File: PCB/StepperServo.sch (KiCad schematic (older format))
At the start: 78 parts, among them P1 Conn_01x06, P2 Conn_01x04, P4 Conn_01x08, P5 Conn_01x02, U1 BNOR11, U2 A4950E, U3 EL-0631, U4 A4950E, U5 TLE5012B, U6 EL357NC, U7 STM32F103CBTx, U8 LD1117S33CTR, U9 PCA82C251, Y1 Crystal, p7 Conn_01x08

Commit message: Added misssing footprints to pcb
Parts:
- U1: footprint (none) -> Package_TO_SOT_SMD:SOT-23-6
- U8: footprint digikey-footprints:SOT-223 -> Package_TO_SOT_SMD:SOT-223; symbol StepperServo-rescue:LD1117S33CTR-dk_PMIC-Voltage-Regulators-Linear-BTTS57Bv2-rescue -> StepperServo-rescue:LD1117S33CTR-dk_PMIC-Voltage-Regulators-Linear
- Y1: footprint (none) -> Crystal:Crystal_SMD_EuroQuartz_MT-4Pin_3.2x2.5mm_HandSoldering; symbol StepperServo-rescue:Crystal-Device-BTTS57Bv2-rescue -> StepperServo-rescue:Crystal-Device
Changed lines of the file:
@@
 Text GLabel 7300 4000 0    50   Input ~ 0
 MICROSTEP1_SW
-Text GLabel 10750 2450 2    50   Input ~ 0
-STP_IN
-Text GLabel 10750 2600 2    50   Input ~ 0
-DIR_IN
-Text GLabel 10300 3400 2    50   Input ~ 0
-EN_IN
 Text GLabel 7300 4200 0    50   Output ~ 0
 OLED_CS
@@
 Text GLabel 7300 3600 0    50   Input ~ 0
 motordriverU4#3
-$Comp
-L StepperServo-rescue:R-Device-BTTS57Bv2-rescue R5
-U 1 1 60AA734D
-P 9500 3050
-F 0 "R5" V 9600 3050 50  0000 C CNN
-F 1 "?R" V 9500 3050 50  0000 C CNN
-F 2 "Resistor_SMD:R_0603_1608Metric" V 9430 3050 50  0001 C CNN
-F 3 "~" H 9500 3050 50  0001 C CNN
-	1    9500 3050
-	-1   0    0    1
-$EndComp
-$Comp
-L StepperServo-rescue:R-Device-BTTS57Bv2-rescue R12
-U 1 1 60AC6CB6
-P 10150 3400
-F 0 "R12" V 10250 3400 50  0000 C CNN
-F 1 "?R" V 10150 3400 50  0000 C CNN
-F 2 "Resistor_SMD:R_0805_2012Metric" V 10080 3400 50  0001 C CNN
-F 3 "~" H 10150 3400 50  0001 C CNN
-	1    10150 3400
-	0    -1   -1   0
-$EndComp
-Connection ~ 9500 3200
-Wire Wire Line
-	9500 3200 9600 3200
 Text GLabel 8050 1550 1    50   Input ~ 0
 VDD
@@
 	8100 1650 8100 1700
 Wire Wire Line
-	8600 3200 9500 3200
-Wire Wire Line
 	8050 1650 8050 1550
 Connection ~ 8050 1650
@@
 Wire Wire Line
 	7900 1650 8000 1650
-Text GLabel 9500 2900 1    50   Input ~ 0
-VDD
-Text GLabel 9600 3400 0    50   Input ~ 0
-VSS
 Wire Wire Line
 	8100 1650 8200 1650
@@
 	8200 1650 8200 1700
 Connection ~ 8100 1650
-$Comp
-L StepperServo-rescue:R-Device-BTTS57Bv2-rescue R9
-U 1 1 60ACF7F8
-P 10600 2600
-F 0 "R9" V 10700 2600 50  0000 C CNN
-F 1 "?R" V 10600 2600 50  0000 C CNN
-F 2 "Resistor_SMD:R_0805_2012Metric" V 10530 2600 50  0001 C CNN
-F 3 "~" H 10600 2600 50  0001 C CNN
-	1    10600 2600
-	0    -1   -1   0
-$EndComp
-$Comp
-L StepperServo-rescue:R-Device-BTTS57Bv2-rescue R3
-U 1 1 60AD1627
-P 10600 2450
-F 0 "R3" V 10700 2450 50  0000 C CNN
-F 1 "?R" V 10600 2500 50  0000 C CNN
-F 2 "Resistor_SMD:R_0805_2012Metric" V 10530 2450 50  0001 C CNN
-F 3 "~" H 10600 2450 50  0001 C CNN
-	1    10600 2450
-	0    -1   -1   0
-$EndComp
-$Comp
-L StepperServo-rescue:R-Device-BTTS57Bv2-rescue R8
-U 1 1 60AEAB54
-P 9600 2200
-F 0 "R8" V 9700 2200 50  0000 C CNN
-F 1 "?R" V 9600 2200 50  0000 C CNN
-F 2 "Resistor_SMD:R_0603_1608Metric" V 9530 2200 50  0001 C CNN
-F 3 "~" H 9600 2200 50  0001 C CNN
-	1    9600 2200
-	-1   0    0    1
-$EndComp
 $Comp
 L StepperServo-rescue:R-Device-BTTS57Bv2-rescue R15
@@
 Text GLabel 9350 2050 1    50   Input ~ 0
 VDD
-Text GLabel 9600 2050 1    50   Input ~ 0
-VDD
-Text GLabel 9900 2250 0    50   Input ~ 0
-VSS
 $Comp
 L StepperServo-rescue:LED-Device-BTTS57Bv2-rescue D4
@@
 	1    0    0    -1
 $EndComp
-$Comp
-L el-0631:EL-0631 U3
-U 1 1 60A729DF
-P 10350 3050
-F 0 "U3" H 10525 4075 50  0000 C CNN
-F 1 "EL-0631" H 10525 3984 50  0000 C CNN
-F 2 "Package_SO:SOP-8_3.9x4.9mm_P1.27mm" H 9990 2730 50  0001 C CNN
-F 3 "" H 9990 2730 50  0001 C CNN
-	1    10350 3050
-	-1   0    0    -1
-$EndComp
 Wire Wire Line
 	9350 2350 9350 2450
-$Comp
-L el-0631:EL357NC U6
-U 1 1 60AC06ED
-P 9850 3550
-F 0 "U6" H 9900 4125 50  0000 C CNN
-F 1 "EL357NC" H 9900 4034 50  0000 C CNN
-F 2 "Package_SO:SOP-4_3.8x4.1mm_P2.54mm" H 9850 3550 50  0001 C CNN
-F 3 "" H 9850 3550 50  0001 C CNN
-	1    9850 3550
-	-1   0    0    -1
-$EndComp
-Wire Wire Line
-	9600 2350 9600 2600
 $Comp
 L StepperServo-rescue:C-Device-BTTS57Bv2-rescue C3
@@
 $EndComp
 $Comp
-L StepperServo-rescue:Crystal-Device-BTTS57Bv2-rescue Y1
+L StepperServo-rescue:Crystal-Device Y1
 U 1 1 60B8D3A3
 P 5000 2350
 F 0 "Y1" H 5000 2618 50  0000 C CNN
 F 1 "Crystal" H 5000 2527 50  0000 C CNN
-F 2 "" H 5000 2350 50  0001 C CNN
+F 2 "Crystal:Crystal_SMD_EuroQuartz_MT-4Pin_3.2x2.5mm_HandSoldering" H 5000 2350 50  0001 C CNN
 F 3 "~" H 5000 2350 50  0001 C CNN
 	1    5000 2350
@@
 $EndComp
 $Comp
-L StepperServo-rescue:LD1117S33CTR-dk_PMIC-Voltage-Regulators-Linear-BTTS57Bv2-rescue U8
+L StepperServo-rescue:LD1117S33CTR-dk_PMIC-Voltage-Regulators-Linear U8
 U 1 1 60BA0B17
 P 1500 4100
 F 0 "U8" H 1550 4387 60  0000 C CNN
 F 1 "LD1117S33CTR" H 1550 4281 60  0000 C CNN
-F 2 "digikey-footprints:SOT-223" H 1700 4300 60  0001 L CNN
+F 2 "Package_TO_SOT_SMD:SOT-223" H 1700 4300 60  0000 L CNN
 F 3 "http://www.st.com/content/ccc/resource/technical/document/datasheet/99/3b/7d/91/91/51/4b/be/CD00000544.pdf/files/CD00000544.pdf/jcr:content/translations/en.CD00000544.pdf" H 1700 4400 60  0001 L CNN
 F 4 "497-1241-1-ND" H 1700 4500 60  0001 L CNN "Digi-Key_PN"
@@
 F 0 "U1" H 2500 6025 50  0000 C CNN
 F 1 "BNOR11" H 2500 5934 50  0000 C CNN
-F 2 "" H 2450 5450 50  0001 C CNN
+F 2 "Package_TO_SOT_SMD:SOT-23-6" H 2450 5450 50  0001 C CNN
 F 3 "" H 2450 5450 50  0001 C CNN
 	1    2450 5450
@@
 	9150 2450 9350 2450
 Wire Wire Line
-	9350 2450 9900 2450
-Connection ~ 9350 2450
-Wire Wire Line
 	9300 3100 9300 2600
-Wire Wire Line
-	9300 2600 9600 2600
-Wire Wire Line
-	9600 2600 9900 2600
-Connection ~ 9600 2600
 $Comp
 L Mechanical:MountingHole_Pad H1
@@
 Wire Wire Line
 	2300 5900 2300 6050
-Text GLabel 9900 2800 0    50   Input ~ 0
-VDD
 Text GLabel 7500 6200 0    50   Input ~ 0
+com
+Wire Wire Line
+	8600 3000 9150 3000
+Wire Wire Line
+	8600 3100 9300 3100
+Connection ~ 9350 2450
+Text GLabel 10450 2800 2    50   Input ~ 0
+com
+Text GLabel 10450 2250 2    50   Input ~ 0
 com
 Text GLabel 10000 3200 2    50   Input ~ 0
 com
-Text GLabel 10450 2250 2    50   Input ~ 0
-com
-Text GLabel 10450 2800 2    50   Input ~ 0
-com
-Wire Wire Line
-	8600 3000 9150 3000
-Wire Wire Line
-	8600 3100 9300 3100
+Text GLabel 9900 2800 0    50   Input ~ 0
+VDD
+Connection ~ 9600 2600
+Wire Wire Line
+	9600 2600 9900 2600
+Wire Wire Line
+	9300 2600 9600 2600
+Wire Wire Line
+	9350 2450 9900 2450
+Wire Wire Line
+	9600 2350 9600 2600
+$Comp
+L el-0631:EL357NC U6
+U 1 1 60AC06ED
+P 9850 3550
+F 0 "U6" H 9900 4125 50  0000 C CNN
+F 1 "EL357NC" H 9900 4034 50  0000 C CNN
+F 2 "Package_SO:SOP-4_3.8x4.1mm_P2.54mm" H 9850 3550 50  0001 C CNN
+F 3 "" H 9850 3550 50  0001 C CNN
+	1    9850 3550
+	-1   0    0    -1
+$EndComp
+$Comp
+L el-0631:EL-0631 U3
+U 1 1 60A729DF
+P 10350 3050
+F 0 "U3" H 10525 4075 50  0000 C CNN
+F 1 "EL-0631" H 10525 3984 50  0000 C CNN
+F 2 "Package_SO:SOP-8_3.9x4.9mm_P1.27mm" H 9990 2730 50  0001 C CNN
+F 3 "" H 9990 2730 50  0001 C CNN
+	1    10350 3050
+	-1   0    0    -1
+$EndComp
+Text GLabel 9900 2250 0    50   Input ~ 0
+VSS
+Text GLabel 9600 2050 1    50   Input ~ 0
+VDD
+$Comp
+L StepperServo-rescue:R-Device-BTTS57Bv2-rescue R8
+U 1 1 60AEAB54
+P 9600 2200
+F 0 "R8" V 9700 2200 50  0000 C CNN
+F 1 "?R" V 9600 2200 50  0000 C CNN
+F 2 "Resistor_SMD:R_0603_1608Metric" V 9530 2200 50  0001 C CNN
+F 3 "~" H 9600 2200 50  0001 C CNN
+	1    9600 2200
+	-1   0    0    1
+$EndComp
+$Comp
+L StepperServo-rescue:R-Device-BTTS57Bv2-rescue R3
+U 1 1 60AD1627
+P 10600 2450
+F 0 "R3" V 10700 2450 50  0000 C CNN
+F 1 "?R" V 10600 2500 50  0000 C CNN
+F 2 "Resistor_SMD:R_0805_2012Metric" V 10530 2450 50  0001 C CNN
+F 3 "~" H 10600 2450 50  0001 C CNN
+	1    10600 2450
+	0    -1   -1   0
+$EndComp
+$Comp
+L StepperServo-rescue:R-Device-BTTS57Bv2-rescue R9
+U 1 1 60ACF7F8
+P 10600 2600
+F 0 "R9" V 10700 2600 50  0000 C CNN
+F 1 "?R" V 10600 2600 50  0000 C CNN
+F 2 "Resistor_SMD:R_0805_2012Metric" V 10530 2600 50  0001 C CNN
+F 3 "~" H 10600 2600 50  0001 C CNN
+	1    10600 2600
+	0    -1   -1   0
+$EndComp
+Text GLabel 9600 3400 0    50   Input ~ 0
+VSS
+Text GLabel 9500 2900 1    50   Input ~ 0
+VDD
+Wire Wire Line
+	8600 3200 9500 3200
+Wire Wire Line
+	9500 3200 9600 3200
+Connection ~ 9500 3200
+$Comp
+L StepperServo-rescue:R-Device-BTTS57Bv2-rescue R12
+U 1 1 60AC6CB6
+P 10150 3400
+F 0 "R12" V 10250 3400 50  0000 C CNN
+F 1 "?R" V 10150 3400 50  0000 C CNN
+F 2 "Resistor_SMD:R_0805_2012Metric" V 10080 3400 50  0001 C CNN
+F 3 "~" H 10150 3400 50  0001 C CNN
+	1    10150 3400
+	0    -1   -1   0
+$EndComp
+$Comp
+L StepperServo-rescue:R-Device-BTTS57Bv2-rescue R5
+U 1 1 60AA734D
+P 9500 3050
+F 0 "R5" V 9600 3050 50  0000 C CNN
+F 1 "?R" V 9500 3050 50  0000 C CNN
+F 2 "Resistor_SMD:R_0603_1608Metric" V 9430 3050 50  0001 C CNN
+F 3 "~" H 9500 3050 50  0001 C CNN
+	1    9500 3050
+	-1   0    0    1
+$EndComp
+Text GLabel 10300 3400 2    50   Input ~ 0
+EN_IN
+Text GLabel 10750 2600 2    50   Input ~ 0
+DIR_IN
+Text GLabel 10750 2450 2    50   Input ~ 0
+STP_IN
 $EndSCHEMATC

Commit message: Removed dir, step, enable
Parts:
- removed R12, R3, R9: ?R, Resistor_SMD:R_0805_2012Metric, symbol StepperServo-rescue:R-Device-BTTS57Bv2-rescue
- removed R15, R5, R8: ?R, Resistor_SMD:R_0603_1608Metric, symbol StepperServo-rescue:R-Device-BTTS57Bv2-rescue
- removed U3: EL-0631, Package_SO:SOP-8_3.9x4.9mm_P1.27mm, symbol el-0631:EL-0631
- removed U6: EL357NC, Package_SO:SOP-4_3.8x4.1mm_P2.54mm, symbol el-0631:EL357NC
- P1: footprint Connector_JST:JST_XH_B6B-XH-A_1x06_P2.50mm_Vertical -> Connector_JST:JST_XH_B2B-XH-A_1x02_P2.50mm_Vertical; symbol StepperServo-rescue:Conn_01x06-Connector_Generic-BTTS57Bv2-rescue -> Connector_Generic:Conn_01x02
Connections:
- net DIR_IN is gone; now on net GND: P1.1 (Pin_1)
- net STP_IN is gone; now on net VMOT: P1.2 (Pin_2)
- net GND: no longer P1.4 (Pin_4)
- net VMOT: no longer P1.6 (Pin_6)
- removed net EN_IN: P1.3 (Pin_3)
- removed net com: P1.5 (Pin_5)
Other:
- moved on the sheet: C13, C16, C2, C4, Next-K2

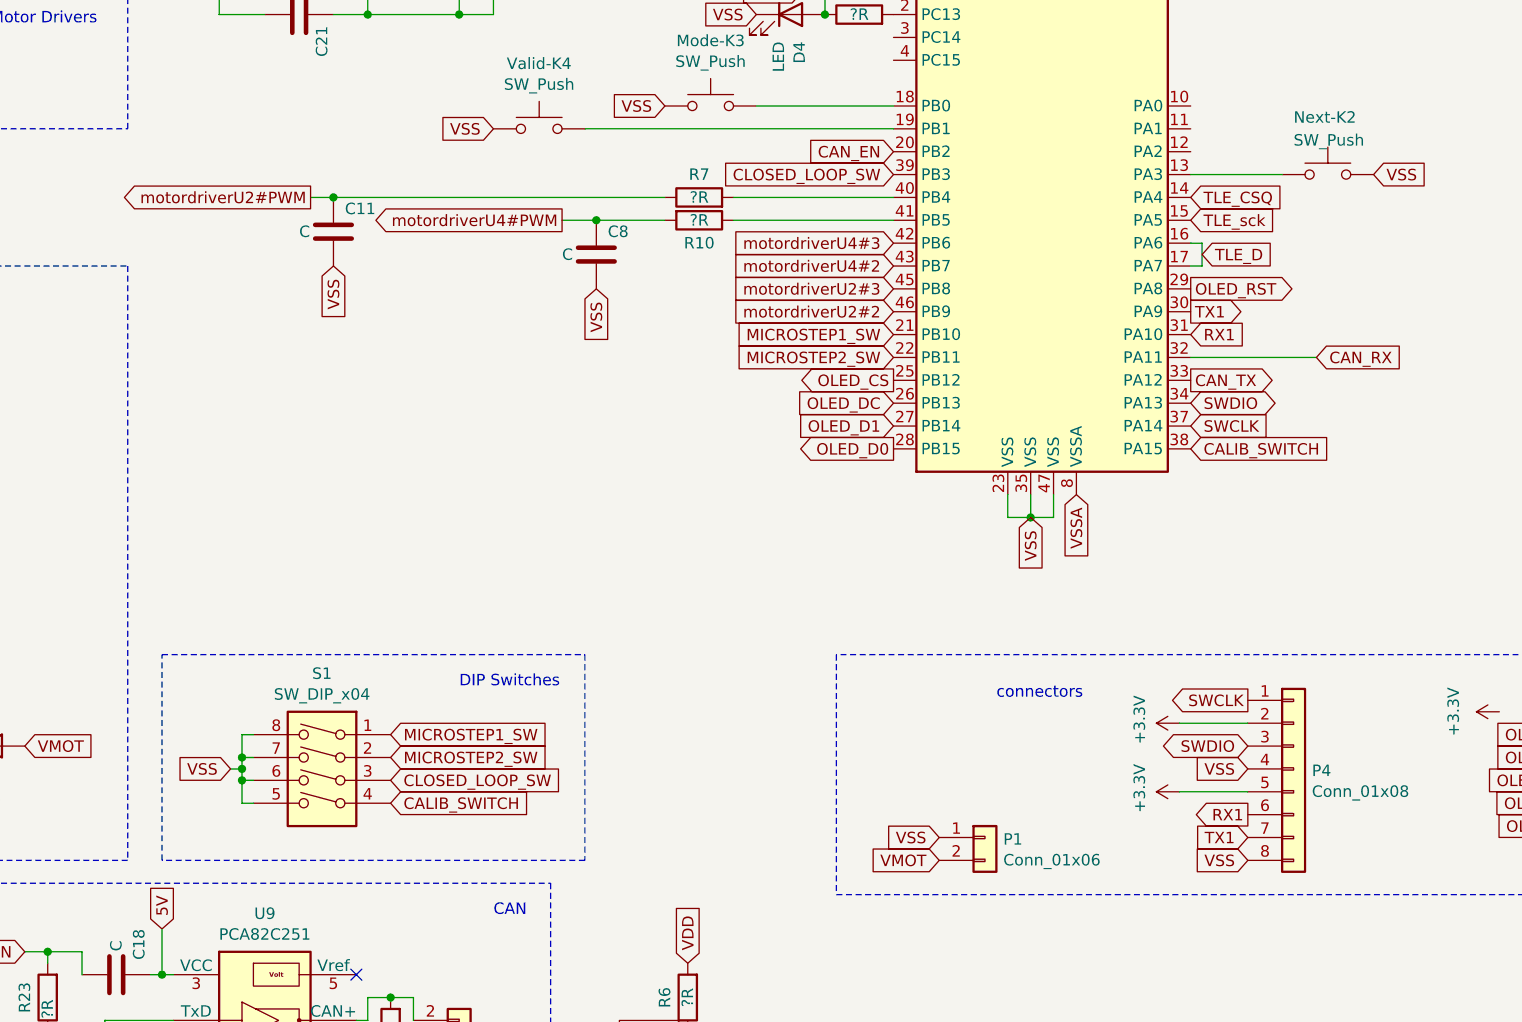
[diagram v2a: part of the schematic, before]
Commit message: Removed dip switches
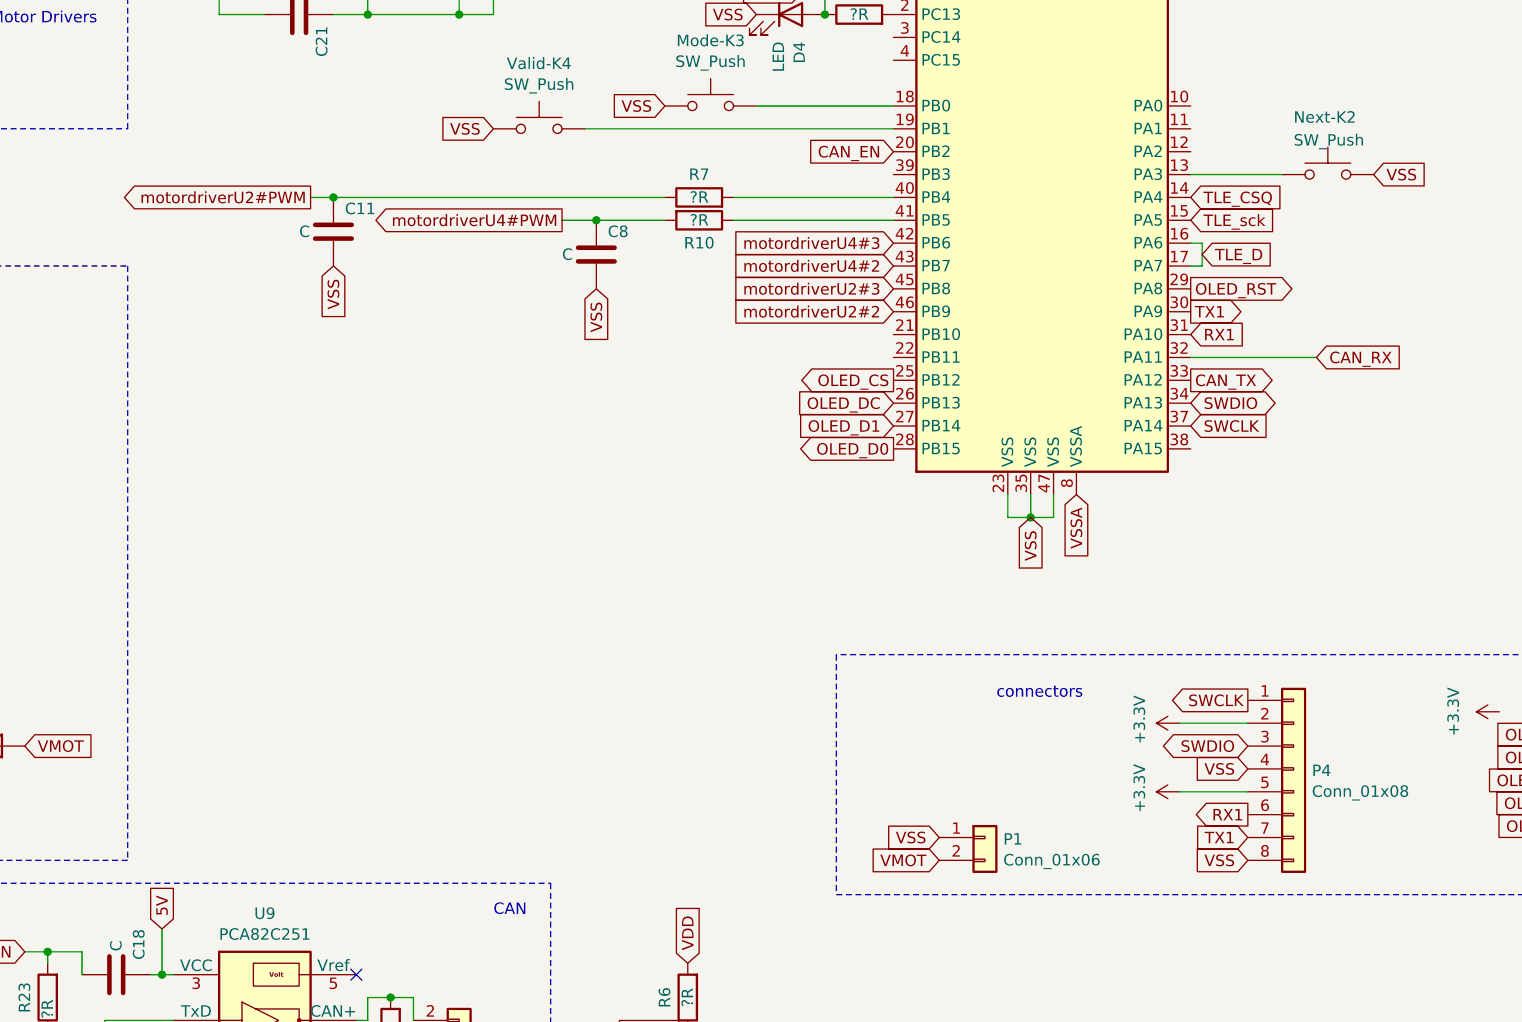
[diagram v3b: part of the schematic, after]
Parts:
- removed S1: SW_DIP_x04, Button_Switch_SMD:SW_DIP_SPSTx04_Slide_KingTek_DSHP04TS_W7.62mm_P1.27mm, symbol StepperServo-rescue:SW_DIP_x04-Switch-BTTS57Bv2-rescue
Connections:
- net CALIB_SWITCH: no longer names the net of U7.38 (PA15)
- net CLOSED_LOOP_SW: no longer names the net of U7.39 (PB3)
- net MICROSTEP1_SW: no longer names the net of U7.21 (PB10)
- net MICROSTEP2_SW: no longer names the net of U7.22 (PB11)
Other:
- note removed: "DIP Switches"
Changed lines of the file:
@@
 Text GLabel 4750 3400 0    50   Output ~ 0
 motordriverU2#PWM
-Text GLabel 5100 6050 2    50   Input ~ 0
-CALIB_SWITCH
-Text GLabel 5100 5950 2    50   Input ~ 0
-CLOSED_LOOP_SW
-Text GLabel 7300 4100 0    50   Input ~ 0
-MICROSTEP2_SW
-Text GLabel 7300 4000 0    50   Input ~ 0
-MICROSTEP1_SW
 Text GLabel 7300 4200 0    50   Output ~ 0
 OLED_CS
@@
 Text GLabel 8600 4000 2    50   Input ~ 0
 RX1
-$Comp
-L StepperServo-rescue:SW_DIP_x04-Switch-BTTS57Bv2-rescue S1
-U 1 1 60A6B868
-P 4800 5950
-F 0 "S1" H 4800 6417 50  0000 C CNN
-F 1 "SW_DIP_x04" H 4800 6326 50  0000 C CNN
-F 2 "Button_Switch_SMD:SW_DIP_SPSTx04_Slide_KingTek_DSHP04TS_W7.62mm_P1.27mm" H 4800 5950 50  0001 C CNN
-F 3 "~" H 4800 5950 50  0001 C CNN
-	1    4800 5950
-	-1   0    0    -1
-$EndComp
 Text GLabel 7900 4800 3    50   Input ~ 0
 VSS
@@
 Wire Wire Line
 	7900 4800 8000 4800
-Text GLabel 5100 5750 2    50   Input ~ 0
-MICROSTEP1_SW
-Text GLabel 5100 5850 2    50   Input ~ 0
-MICROSTEP2_SW
 Text GLabel 7300 3900 0    50   Input ~ 0
 motordriverU2#2
@@
 	1    0    0    -1
 $EndComp
-Text GLabel 8600 4500 2    50   Input ~ 0
-CALIB_SWITCH
-Text GLabel 7300 3300 0    50   Input ~ 0
-CLOSED_LOOP_SW
 Wire Wire Line
 	6900 2500 7000 2500
@@
 	7000 2500 7000 2600
 Connection ~ 7000 2600
-Text GLabel 4400 5900 0    50   Input ~ 0
-VSS
-Wire Wire Line
-	4500 5750 4450 5750
-Wire Wire Line
-	4450 5750 4450 5850
-Wire Wire Line
-	4450 5900 4400 5900
-Wire Wire Line
-	4500 5850 4450 5850
-Connection ~ 4450 5850
-Wire Wire Line
-	4450 5850 4450 5900
-Wire Wire Line
-	4500 5950 4450 5950
-Wire Wire Line
-	4450 5950 4450 5900
-Connection ~ 4450 5900
-Wire Wire Line
-	4500 6050 4450 6050
-Wire Wire Line
-	4450 6050 4450 5950
-Connection ~ 4450 5950
 $Comp
 L TLE5012B:TLE5012B U5
@@
 	600  6400 2750 6400
 Wire Notes Line
-	2850 6400 5800 6400
-Wire Notes Line
-	5800 6400 5800 7650
-Wire Notes Line
 	5800 7650 2850 7650
 Wire Notes Line
@@
 Text Notes 5550 6550 0    50   ~ 0
 CAN
-Text Notes 5400 5550 0    50   ~ 0
-DIP Switches
-Wire Notes Line
-	4100 6300 4100 5400
-Wire Notes Line
-	4100 5400 5950 5400
-Wire Notes Line
-	5950 5400 5950 6300
-Wire Notes Line
-	5950 6300 4100 6300
 Text Notes 7750 5600 0    50   ~ 0
 connectors
@@
 Wire Wire Line
 	8200 1650 8750 1650
+Wire Notes Line
+	5800 6400 5800 7650
+Wire Notes Line
+	2850 6400 5800 6400
 $EndSCHEMATC
